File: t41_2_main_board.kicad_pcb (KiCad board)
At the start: 2 copper layers, 100 x 100 mm, 50 parts, among them IC1 74HC125D, J1 Conn_02x08_Odd_Even, J10 SJ-3524-SMT, J11 B2B-XH-A_LF__SN_, J12 SJ-3524-SMT, J13 B3B-XH-A_LF__SN_, J14 B2B-XH-A_LF__SN_, J15 B4B-XH-A_LF__SN_, J16 B3B-XH-A_LF__SN_, J2 Conn_02x05_Odd_Even, J3 Conn_02x05_Odd_Even, J4 Conn_02x05_Odd_Even, J5 Conn_02x05_Odd_Even, J6 SJ-3524-SMT, J7 SJ-3524-SMT, J8 SJ-3524-SMT, J9 B3B-XH-A_LF__SN_, U1 Teensy4.1

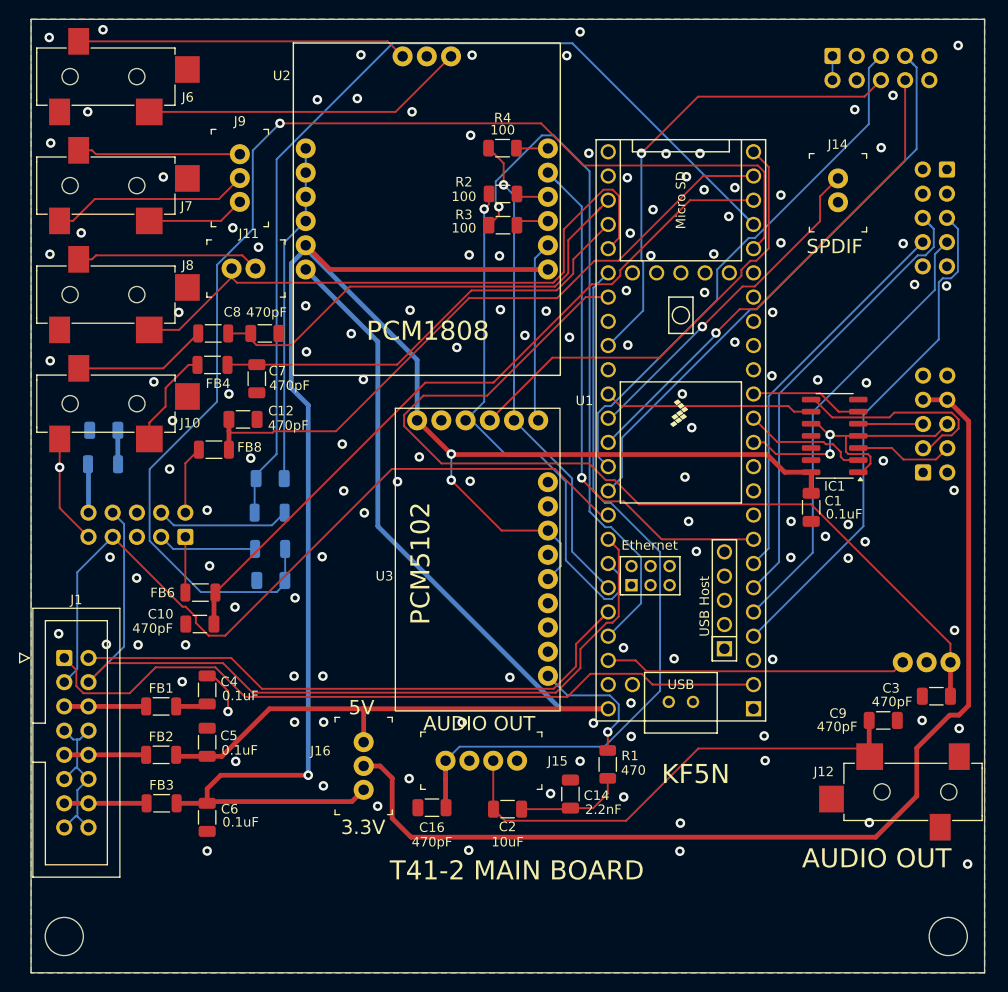
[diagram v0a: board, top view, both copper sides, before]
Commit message: V1.1 routes 0.  Needs further clean-up.
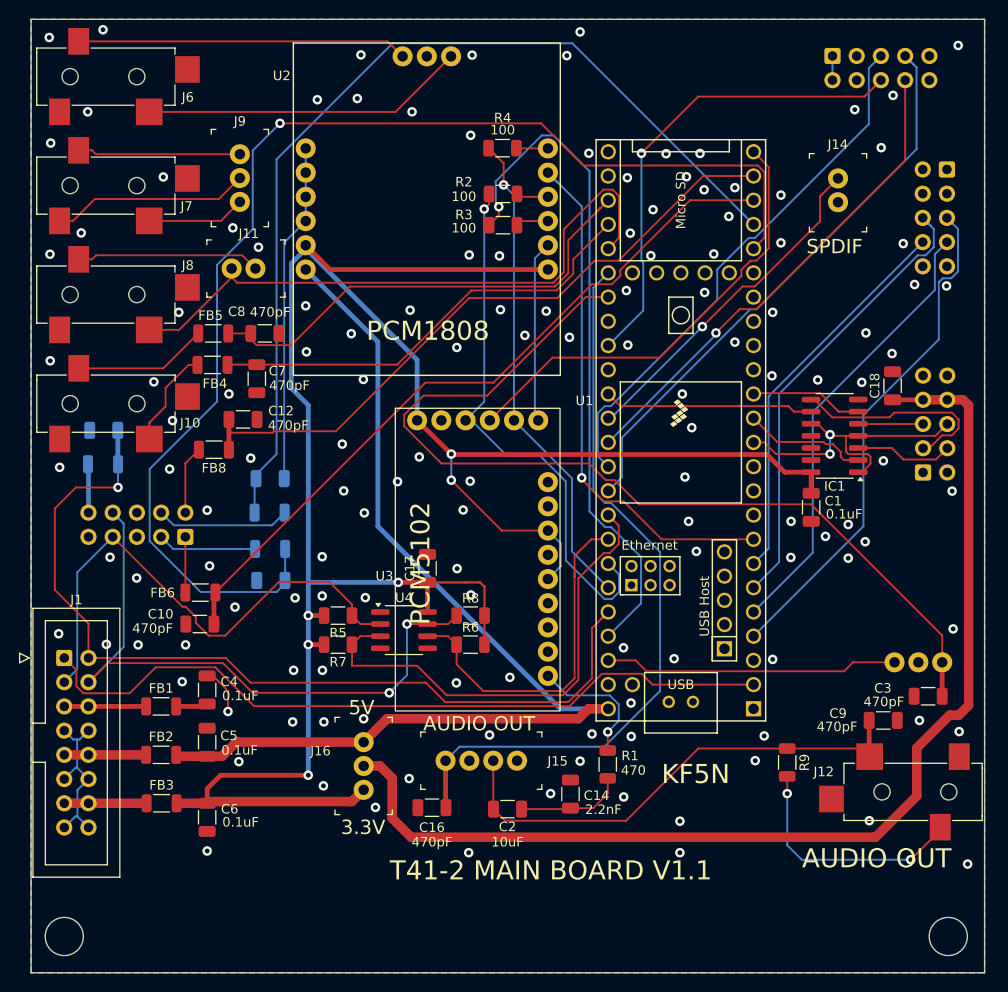
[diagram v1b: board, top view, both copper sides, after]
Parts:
- added C17: 0.1uF, Capacitor_SMD:C_1206_3216Metric, F.Cu at (138.1, 111.4)
- added C18: 0.1uF, Capacitor_SMD:C_1206_3216Metric, F.Cu at (186.9, 92.2)
- added R5: 1.0k, Resistor_SMD:R_1206_3216Metric, F.Cu at (128.7, 116.3)
- added R6: 4.7k, Resistor_SMD:R_1206_3216Metric, F.Cu at (142.6, 119.4)
- added R7: 4.7k, Resistor_SMD:R_1206_3216Metric, F.Cu at (128.7, 119.4)
- added R8: 1.0k, Resistor_SMD:R_1206_3216Metric, F.Cu at (142.6, 116.3)
- added R9: 0, Resistor_SMD:R_1206_3216Metric, F.Cu at (175.8, 131.8)
- added U4: P82B715DR, Package_SO:SOIC-8_3.9x4.9mm_P1.27mm, F.Cu at (135.6, 117.9)
- moved J13 0.87 mm to (192.1, 121.2)
- moved C3 0.86 mm to (190.6, 124.8)
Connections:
- net Net-(J11-Pad2) renamed /MIC_AUDIO
- C15 pad 1: /RXTX -> /TXRX
- FB10 pad 2: /RXTX -> /TXRX
- J1 pad 3: /SDA -> /SDA_OUT1
- J1 pad 4: /SCL -> /SCL_OUT1
- J11 pad 1: /PTT -> GND
- J12 pad 3: unconnected-(J12-Pad3) -> Net-(J12-Pad3)
- J3 pad 7: /SDA -> /SDA_OUT1
- J3 pad 8: /SCL -> /SCL_OUT1
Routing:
- net /SCL_OUT1: track 0.00 -> 67.0 mm, vias 0 -> 2
- net /SDA_OUT1: track 0.00 -> 54.9 mm
- net /SCL: track 90.6 -> 37.1 mm
- net /TXRX: track 60.9 -> 94.5 mm, vias 0 -> 1
- net /SDA: track 83.2 -> 51.1 mm
- net /3_3V_FIL: track 207.4 -> 238.5 mm, vias 3 -> 6
- net Net-(J12-Pad3): track 0.00 -> 25.5 mm, vias 0 -> 2
- net GND: track 93.8 -> 82.2 mm, vias 128 -> 137
- net /DISP_PWR: track 113.2 -> 117.4 mm
- net /RXTX: track 3.57 -> 0.00 mm
- net /5V_FIL: track 113.1 -> 109.6 mm
- net /SWITCH_MATRIX: track 100.9 -> 99.6 mm
- net /RESET: track 78.7 -> 79.9 mm
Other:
- board text added: "T41-2 MAIN BOARD V1.1"

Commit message: Fixed schematic route of 3.3 volts and 12 volts to filter connector.
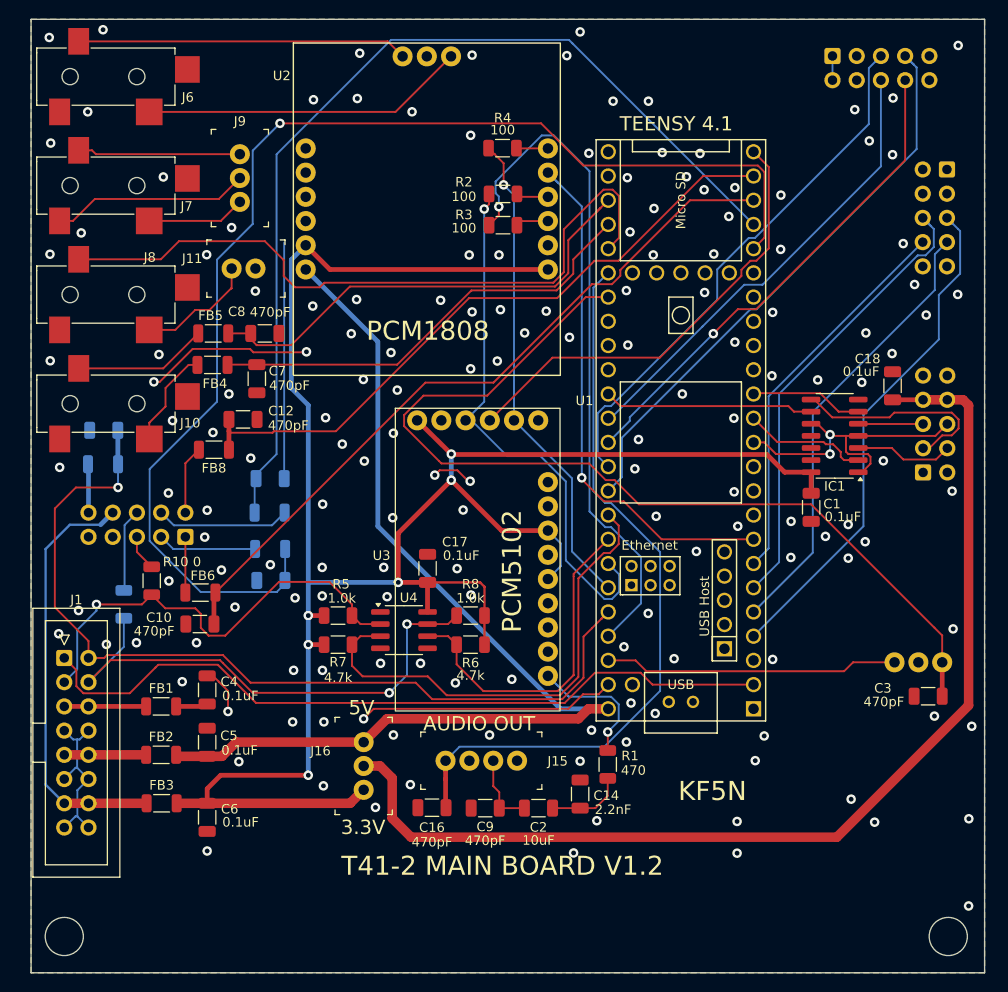
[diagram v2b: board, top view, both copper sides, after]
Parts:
- removed J12: SJ-3524-SMT, SJ-3524-SMT:CUI_SJ-3524-SMT
- removed J14: B2B-XH-A_LF__SN_, digikey-footprints:PinHeader_1x2_P2.5mm_Drill1.1mm
- removed R9: 0, Resistor_SMD:R_1206_3216Metric
- added R10: 0, Resistor_SMD:R_1206_3216Metric, F.Cu at (109.2, 112.7)
- added R11: 0, Resistor_SMD:R_1206_3216Metric, B.Cu at (106.2, 115.2)
- moved C9 42.7 mm to (144.1, 136.5), turned to 0 degrees
- moved C2 3.25 mm to (149.7, 136.5)
- moved C14 1.02 mm to (154.1, 135.1)
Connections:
- J11 pad 1: GND -> /MIC_AUDIO
- J11 pad 2: /MIC_AUDIO -> GND
- J3 pad 5: unconnected-(J3-Pin_5-Pad5) -> Net-(J3-Pin_5)
- J3 pad 6: unconnected-(J3-Pin_6-Pad6) -> Net-(J3-Pin_6)
- J3 pad 7: /SDA_OUT1 -> unconnected-(J3-Pin_7-Pad7)
- J3 pad 8: /SCL_OUT1 -> /3_3V_IN
- J8 pad 2: /PTT -> /MIC_AUDIO
- J8 pad 3: /MIC_AUDIO -> /PTT
- U1 pad 33: Net-(J4-Pin_6) -> unconnected-(U1-41_A17-Pad33)
- U1 pad 36: /SPDIF_OUT -> Net-(J4-Pin_6)
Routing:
- net Net-(C2-Pad2): track 53.9 -> 7.87 mm
- net /3_3V_IN: track 8.64 -> 44.7 mm
- net /SPDIF_OUT: track 36.0 -> 0.00 mm, vias 1 -> 0
- net Net-(J12-Pad3): track 25.5 -> 0.00 mm, vias 2 -> 0
- net GND: track 82.2 -> 101.4 mm, vias 137 -> 162
- net /SCL_OUT1: track 67.0 -> 55.7 mm
- net /3_3V_FIL: track 238.5 -> 228.5 mm
- net Net-(J3-Pin_6): track 0.00 -> 8.72 mm
- net /SDA_OUT1: track 54.9 -> 47.2 mm, vias 0 -> 1
- net /PTT: track 66.1 -> 73.6 mm
- net /MIC_AUDIO: track 19.3 -> 12.5 mm
- net Net-(J3-Pin_5): track 0.00 -> 3.78 mm
- net Net-(C14-Pad2): track 11.3 -> 8.15 mm
- net /DISP_PWR: track 117.4 -> 114.4 mm
- net /SCL: track 37.1 -> 35.4 mm
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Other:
- board text added: "T41-2 MAIN BOARD V1.2"
- board text added: "TEENSY 4.1"
- board text removed: "SPDIF"
- board text removed: "T41-2 MAIN BOARD V1.1"

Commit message: Layout re-do probably done.
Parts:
- added C19: 470pF, Capacitor_SMD:C_1206_3216Metric, F.Cu at (120.4, 120.5)
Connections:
- J3 pad 7: unconnected-(J3-Pin_7-Pad7) -> /12V_IN
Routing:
- net /12V_IN: track 8.58 -> 29.8 mm
- net /TXRX: track 93.9 -> 91.0 mm
- net /40MFILTER: track 69.4 -> 71.6 mm
- net GND: track 101.4 -> 103.2 mm
